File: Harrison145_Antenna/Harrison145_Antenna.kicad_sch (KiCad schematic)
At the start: 10 parts, among them J3 AudioJack3, SW1 SW_SPDT

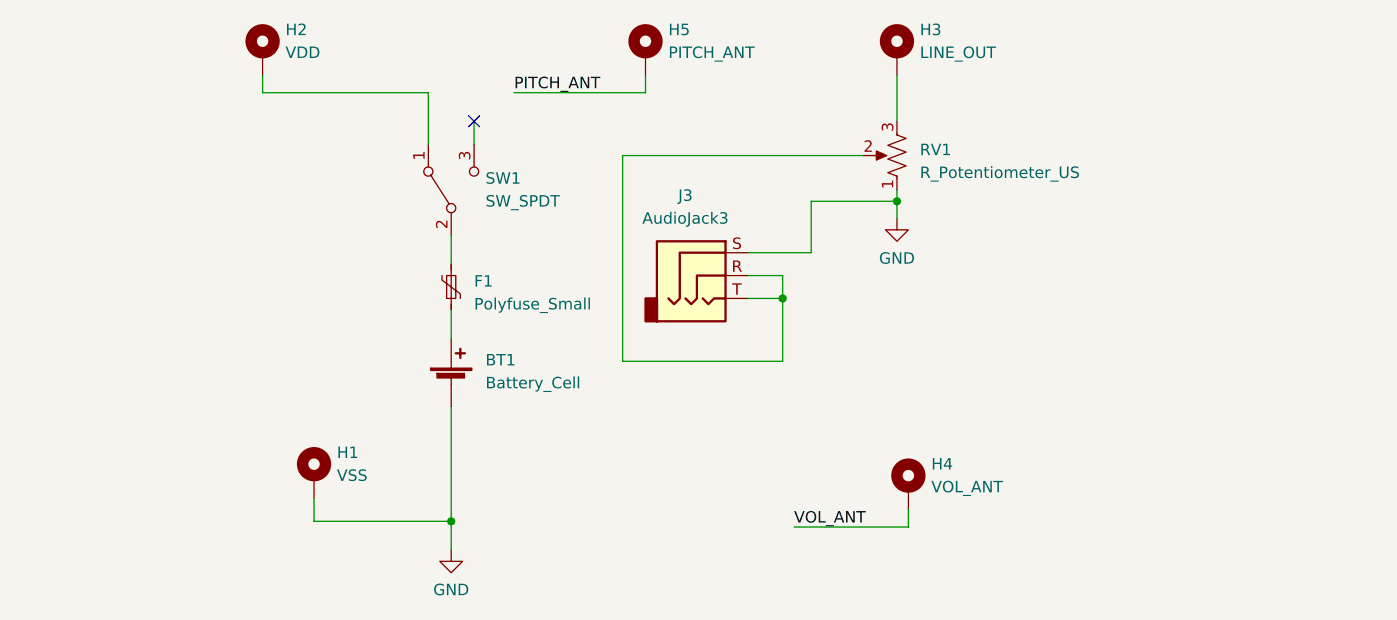
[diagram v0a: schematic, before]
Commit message: Antenna ordered from JLCPCB
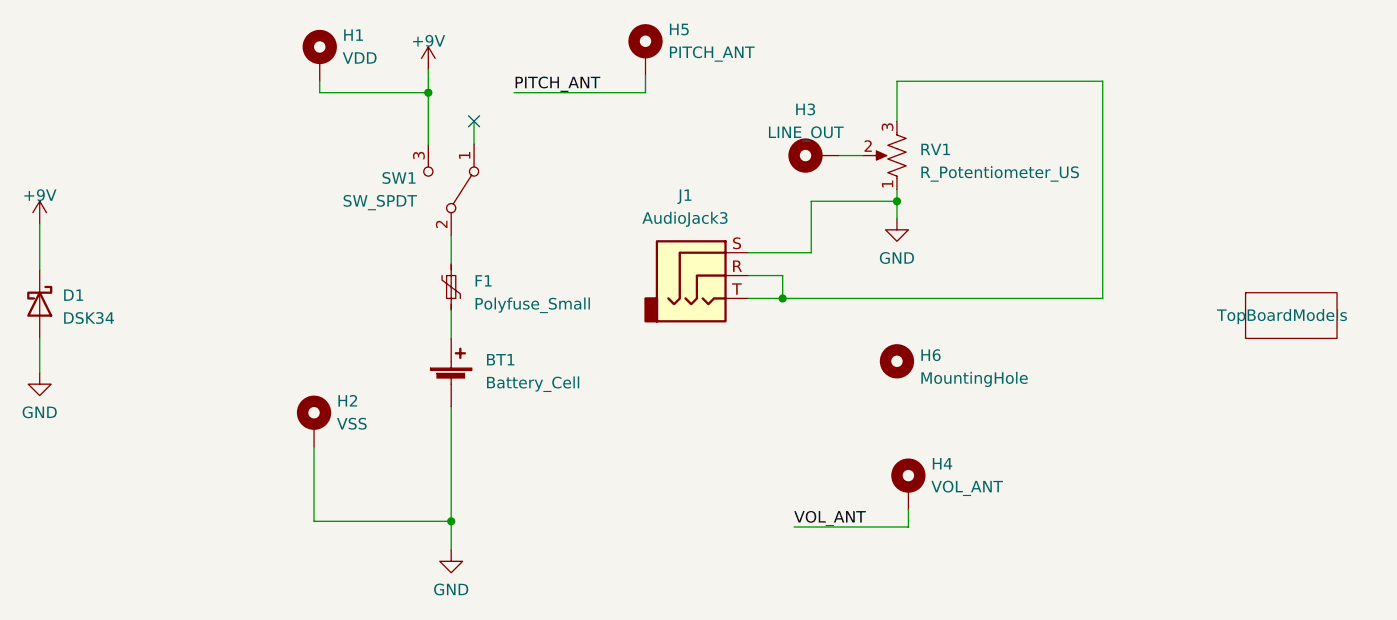
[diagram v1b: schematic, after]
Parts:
- added D1: DSK34, Diode_SMD:D_SOD-123F, symbol Device:D_Schottky
- added H6: MountingHole, Theremin:MicStandHole, symbol Mechanical:MountingHole
- added REF1: TopBoardModels, Theremin:TopBoardModels, symbol Assorted:BOM ITEM
- H1: renamed from H2; footprint Theremin:SMTSO-M4 -> Theremin:SMTSO-M4-6ET
- H2: renamed from H1; footprint Theremin:SMTSO-M4 -> Theremin:SMTSO-M4-6ET
- H3: renamed from H5; value PITCH_ANT -> LINE_OUT; footprint Theremin:SMTSO-M4 -> Theremin:SMTSO-M4-6ET
- H4: renamed from H3; value LINE_OUT -> VOL_ANT; footprint Theremin:SMTSO-M4 -> Theremin:SMTSO-M4-6ET
- H5: renamed from H4; value VOL_ANT -> PITCH_ANT; footprint Theremin:SMTSO-M4 -> Theremin:SMTSO-M4-6ET
- renumbered J3 to J1
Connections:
- net GND: now also D1.2 (A)
- net PITCH_ANT: now also H5.1; no longer H3.1
- net VOL_ANT: now also H4.1; no longer H5.1
- net at J1.R, J1.T: now also RV1.3; no longer RV1.2
- net at SW1.1 (A): no longer H1.1
- net +9V: now reaches SW1.3 (C)
- net +9V: now also H1.1, D1.1 (K)
- new net: H3.1, RV1.2
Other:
- moved on the sheet: H1, H2, H3, H4, H5, SW1
